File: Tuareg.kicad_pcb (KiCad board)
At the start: 4 copper layers, 101.6 x 103.6 mm, 200 parts, among them CON1 ModICE_48, J1 SWD_boctok, P1 VNLD5090e, P2 FAN1100, P3 VNLD5090e, P4 FAN1100, P5 ISO7421D, Q1 BTS3028SDL, Q2 BTS3028SDL, Q3 ISL9V3040, Q4 BTS3028SDL, Q5 ISL9V3040, U1 NCV1117DT, U2 NCV1117ST, U3 MCP6004, U4 MCP6004, U5 LM2903, U6 STM32F410RBTx, U7 24C64, Y1 lfxtal071673, Y2 cx5032ga

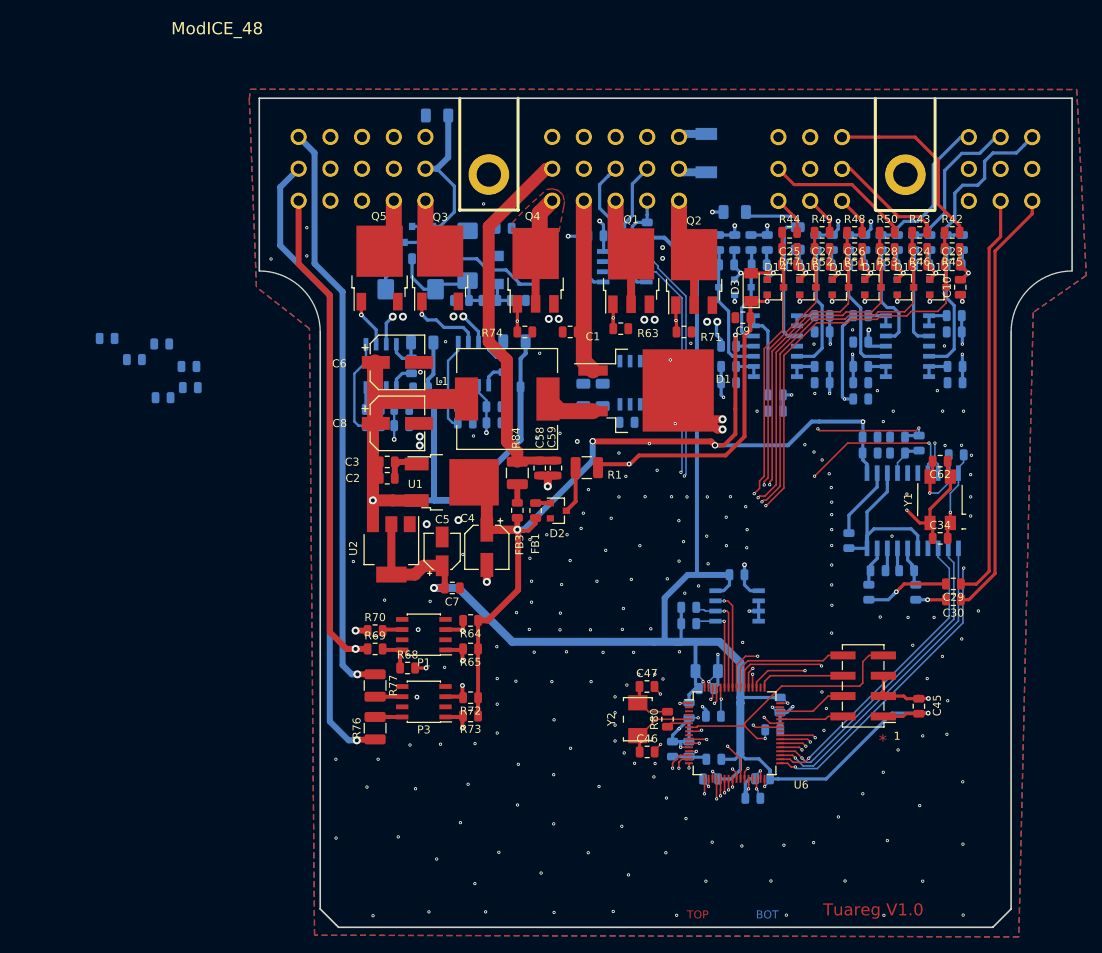
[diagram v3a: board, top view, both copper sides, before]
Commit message: routing discrete vr interface TODO: route "crank" signal
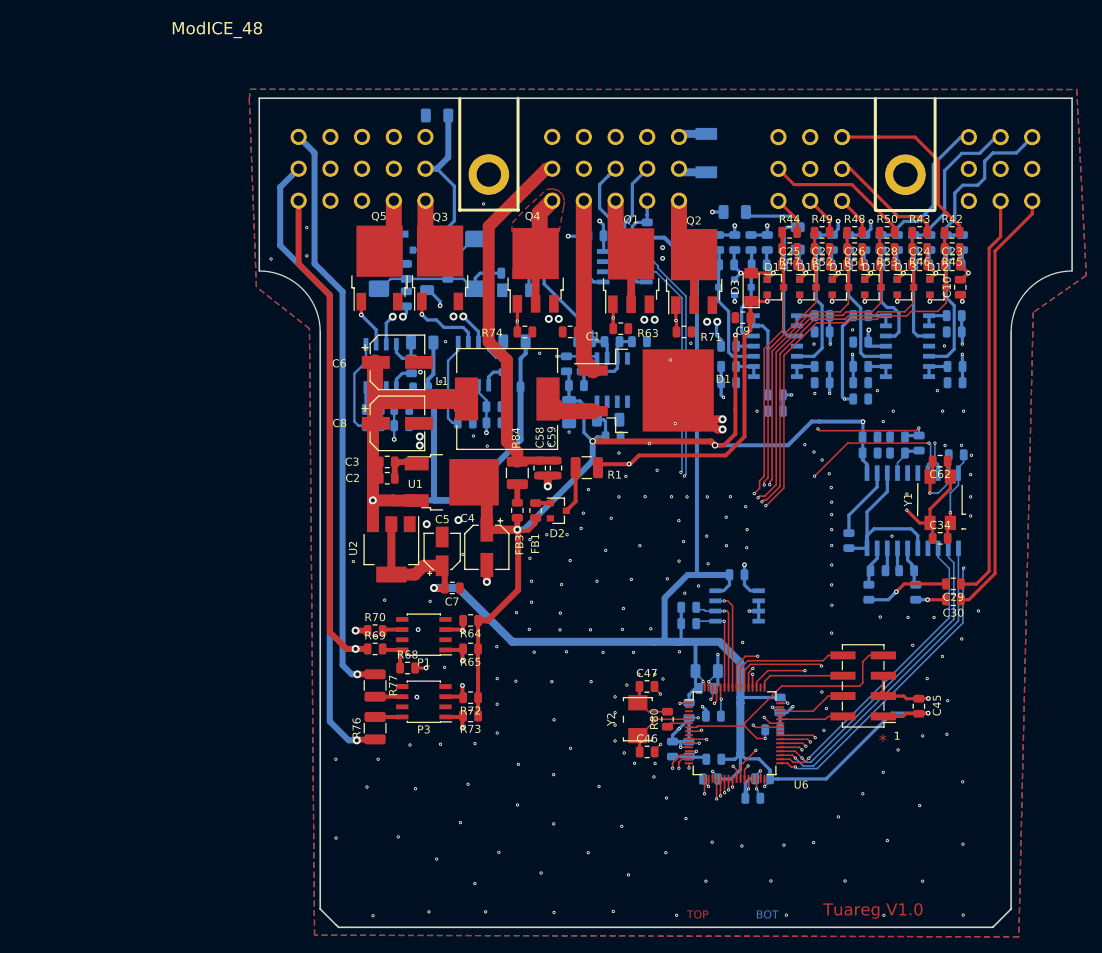
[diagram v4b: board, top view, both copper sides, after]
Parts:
- R35: footprint Resistor_SMD:R_0805_2012Metric -> Resistor_SMD:R_1206_3216Metric
- moved C66 59.7 mm to (121.8, 82.2)
- moved R58 59.7 mm to (125.2, 82.2)
- moved R86 59.5 mm to (118.1, 85.0), turned to 270 degrees
- moved R87 50.6 mm to (116.1, 85.0), turned to 90 degrees
- moved R41 49.6 mm to (118.4, 82.2)
- moved R85 48.5 mm to (117.4, 87.7)
- moved R36 8.86 mm to (101.3, 73.5), turned to 270 degrees
- moved R37 6.89 mm to (96.1, 76.9), turned to 270 degrees
- moved C65 5.08 mm to (92.7, 72.5), turned to 270 degrees
- moved R39 4.14 mm to (108.9, 73.7)
- moved R40 4.09 mm to (112.4, 73.7)
- moved D22 3.50 mm to (109.9, 75.8), turned to 180 degrees
- moved C22 3.17 mm to (121.3, 92.0), turned to 0 degrees
- moved U5 2.89 mm to (121.8, 87.0)
- moved C64 2.80 mm to (116.5, 91.1), turned to 270 degrees
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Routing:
- net /crank: track 66.0 -> 9.48 mm
- net pwr_5v_clamp: track 93.9 -> 120.5 mm, vias 9 -> 10
- net +5V: track 156.5 -> 174.7 mm
- net Net-(C66-Pad1): track 0.00 -> 14.8 mm
- net Net-(C66-Pad2): track 0.00 -> 11.4 mm
- net Net-(C21-Pad1): track 14.3 -> 20.2 mm
- net Net-(C21-Pad2): track 3.98 -> 5.63 mm
- net GND: track 503.6 -> 505.2 mm, vias 236 -> 237

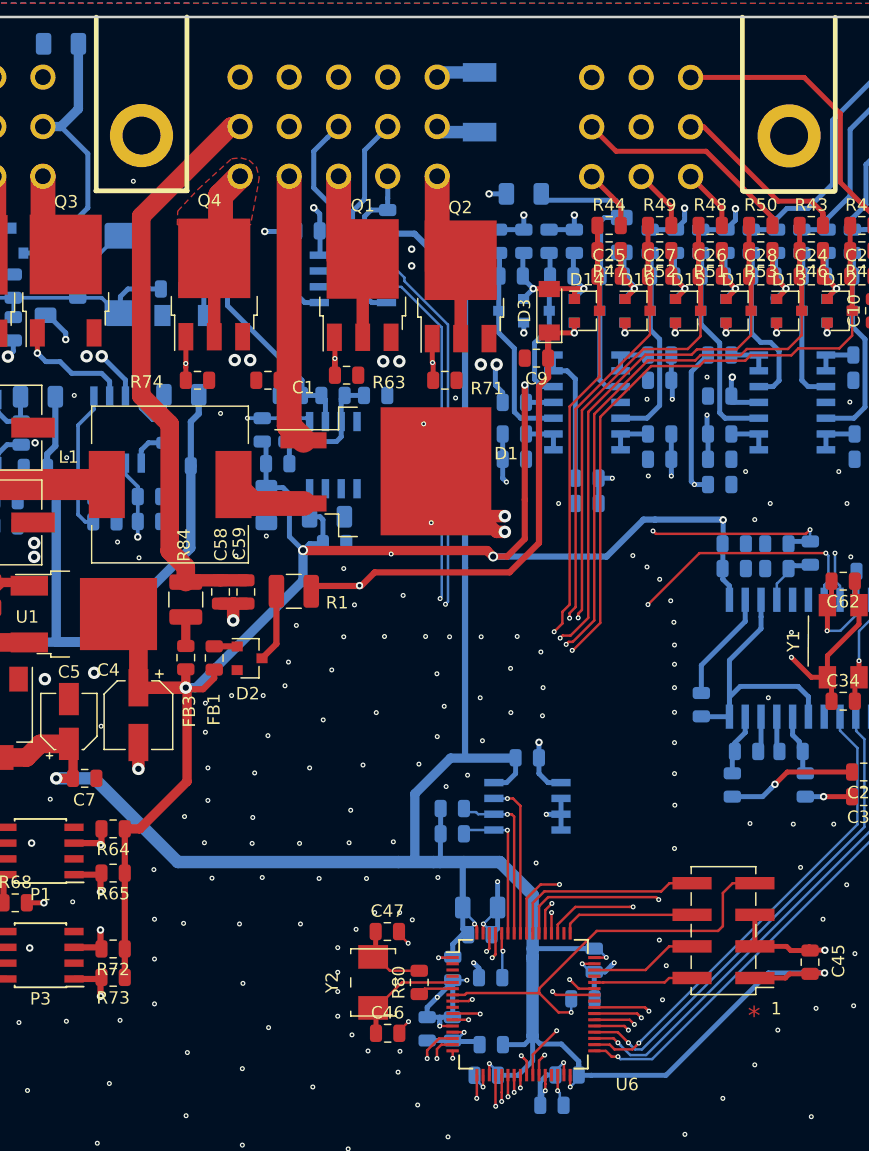
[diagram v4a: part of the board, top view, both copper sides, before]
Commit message: routed crank signal
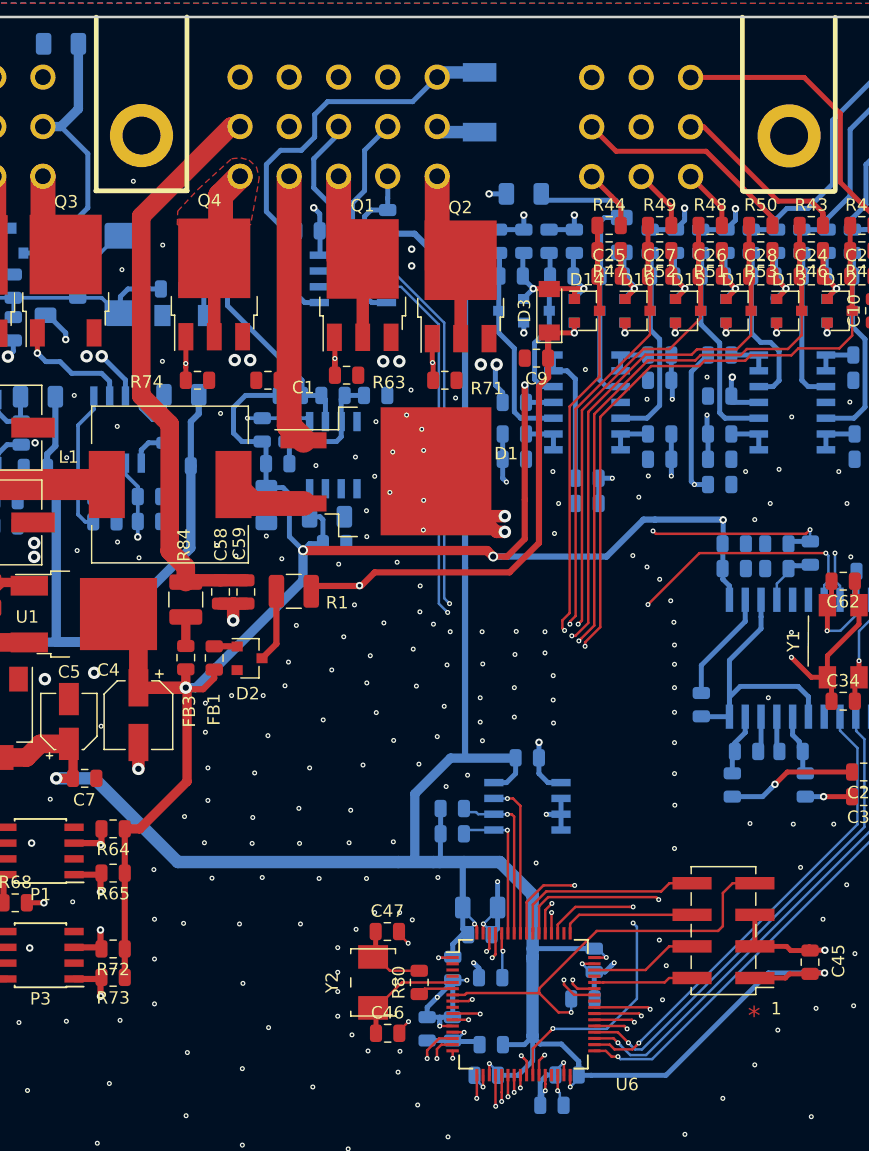
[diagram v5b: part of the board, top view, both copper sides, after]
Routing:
- net /crank: track 9.48 -> 84.9 mm, vias 2 -> 3
- net +5V: track 174.7 -> 183.3 mm, vias 7 -> 6
- net /FUELP: track 78.2 -> 84.3 mm
- net /cpu/USART1_TX: track 77.0 -> 74.1 mm
- net /con_gndi: track 37.3 -> 35.3 mm, vias 1 -> 0
- net /cpu/USART1_RX: track 75.8 -> 74.0 mm
- net /COIL2: track 97.7 -> 96.9 mm
- net /COIL1: track 84.1 -> 83.4 mm
- net /din_spare2: track 69.9 -> 70.4 mm
- net GND: vias 237 -> 275

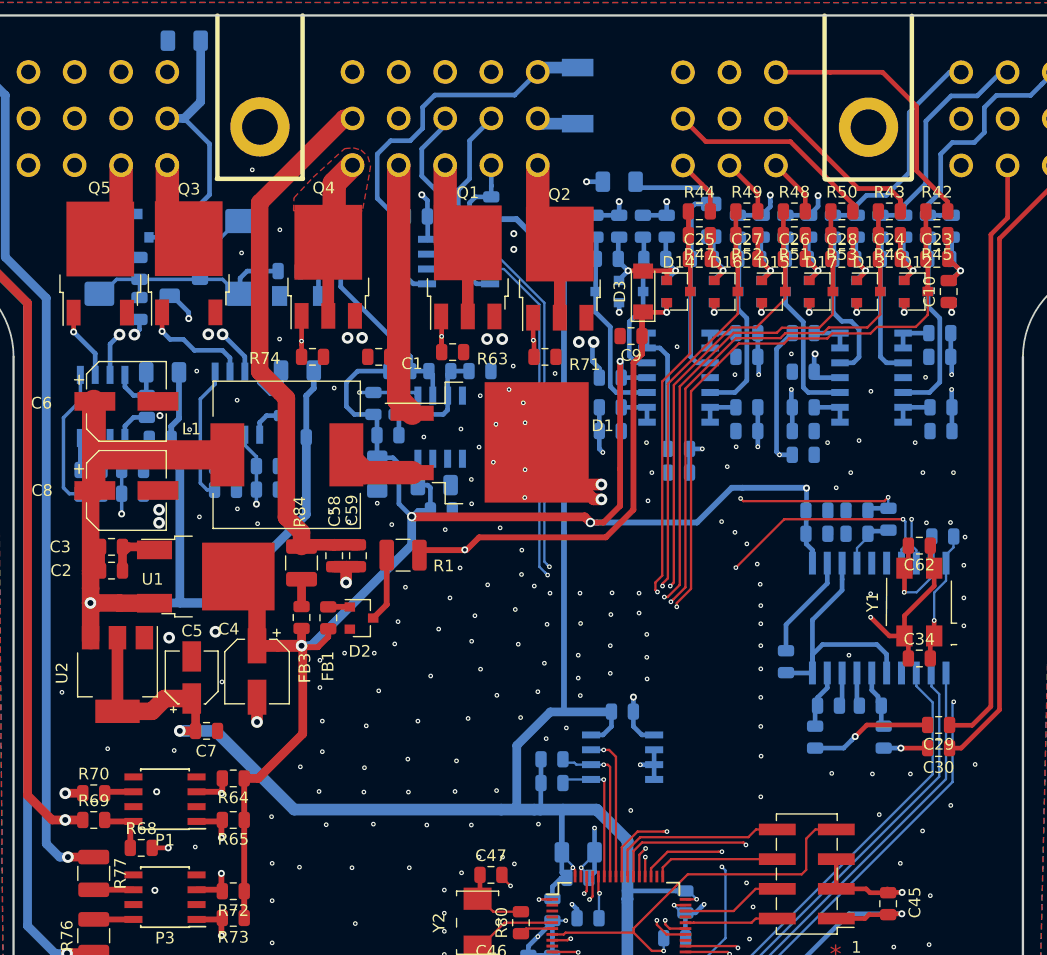
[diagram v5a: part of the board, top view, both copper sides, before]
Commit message: minor design improvements for first series production
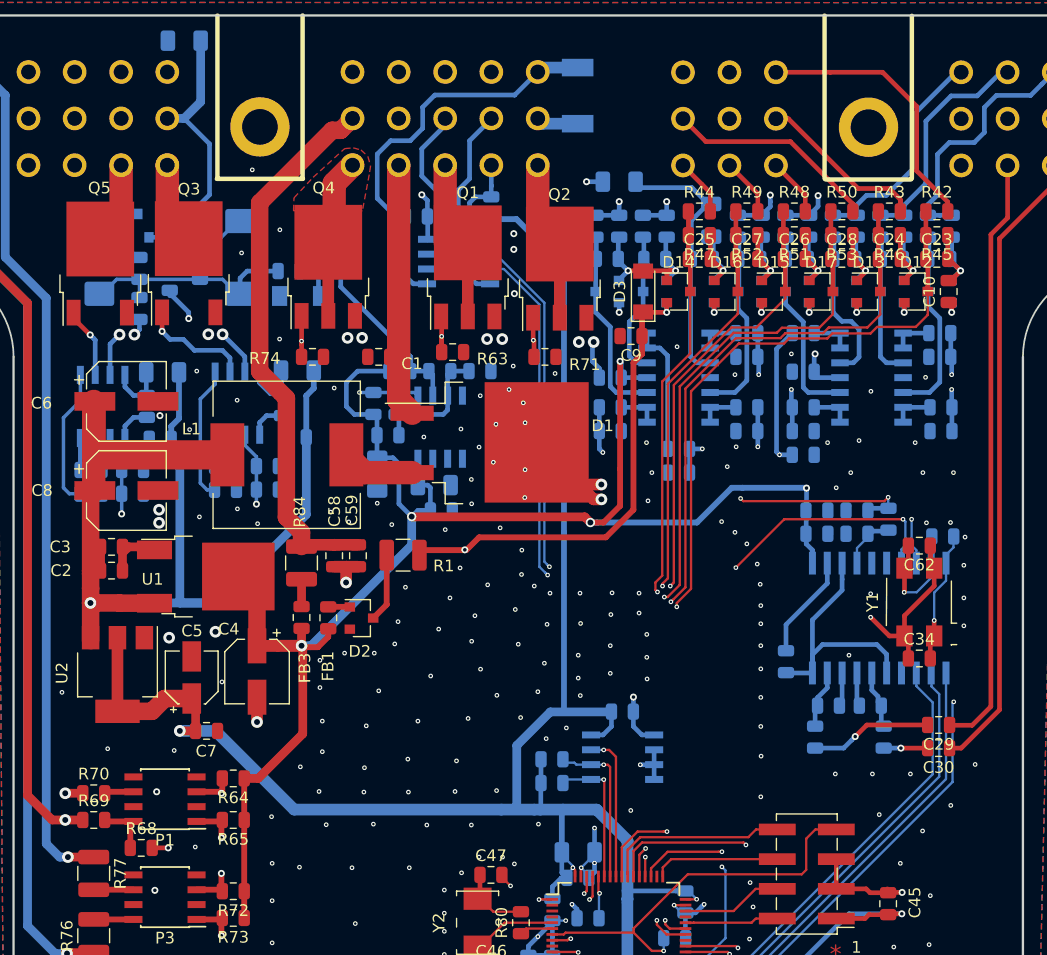
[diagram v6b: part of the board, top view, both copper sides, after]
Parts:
- R35: footprint Resistor_SMD:R_1206_3216Metric -> Resistor_SMD:R_0805_2012Metric
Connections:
- CON1 pad 7: /con_ach1 -> /con_ach8
- CON1 pad 9: /con_ach8 -> /con_ach1
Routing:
- net /con_ach8: track 23.1 -> 41.1 mm
- net /con_ach1: track 26.9 -> 19.3 mm
- net /LAMP: track 46.0 -> 44.4 mm
- net /analog input/bat_in: track 24.3 -> 23.1 mm
- net +12V: track 204.8 -> 203.7 mm
- net /spare_act_2: track 40.1 -> 39.1 mm
- net /spare_act_1: track 44.7 -> 44.0 mm
- net GND: vias 275 -> 277

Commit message: cleaning up
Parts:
- added REF**: OSHW-Logo2_14.6x12mm_Copper, Symbol:OSHW-Logo2_14.6x12mm_Copper, F.Cu at (113.2, 148.0)
- added REF**: KiCad-Logo_5mm_Copper, Symbol:KiCad-Logo_5mm_Copper, F.Cu at (93.9, 150.7)
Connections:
- CON1 pad 36: Net-(CON1-Pad36) -> GND
- CON1 pad 37: Net-(CON1-Pad37) -> GND
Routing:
- net /knock_cs: track 63.6 -> 58.9 mm
- net GND: track 505.2 -> 509.1 mm, vias 277 -> 284
- net /cam: track 77.0 -> 77.8 mm
- net Net-(C33-Pad1): track 22.9 -> 23.5 mm

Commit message: running connection check
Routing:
- net /din_spare1: track 68.9 -> 70.2 mm
- net /con_ach5: track 17.7 -> 16.5 mm
- net GND: track 509.1 -> 509.4 mm, vias 284 -> 283
